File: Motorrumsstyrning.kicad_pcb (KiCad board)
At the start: 4 copper layers, 65 x 60.5 mm, 59 parts, among them J1 SD_Card_Connector, J10 Jumper, J11 Jumper, J12 Jumper, J13 Jumper, J14 Jumper, J15 Jumper, J16 Jumper, J17 Jumper, J18 Jumper, J19 Jumper, J2 Jumper, J20 Jumper, J21 Jumper, J22 Jumper, J23 Screw_Terminal_01x10, J24 Screw_Terminal_01x10, J3 Jumper, J4 Jumper, J5 Jumper, J6 Jumper, J7 Jumper, J8 Jumper, J9 Jumper, Q1 BC337, Q2 BC337, U1 NUCLEO-F303K8, U2 LM1084-5.0, U3 MCP2551-I-P

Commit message: Vidareutveckling
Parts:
- removed G***: LOGO, Vera-MRS-21:Vera-Logo-Small
- removed the J10 at (139.7, 113.0)
- removed the J14 at (144.8, 114.9)
- removed the J15 at (147.3, 114.9)
- removed J16, J17, J18, J19, J20, J21, J22: Jumper, Vera-MRS-21:THT_Jumper
- added J13: Conn_01x11, Connector_PinHeader_2.54mm:PinHeader_1x11_P2.54mm_Vertical, F.Cu at (137.2, 114.9)
- moved JP2 0.13 mm to (144.8, 112.5)
- moved JP3 0.13 mm to (147.3, 112.5)
- moved JP4 0.13 mm to (149.9, 112.5)
- moved JP5 0.13 mm to (152.4, 112.5)
- moved JP6 0.13 mm to (154.9, 112.5)
- moved JP7 0.13 mm to (157.5, 112.5)
- moved JP8 0.13 mm to (160.0, 112.5)
- moved JP9 0.13 mm to (162.6, 112.5)
- renumbered J11 to J10, J12 to J11, J13 to J12, J23 to J14, J24 to J15
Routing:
- net +5V: track 74.9 -> 83.4 mm
- net /USART2_TX: track 32.0 -> 27.1 mm, vias 1 -> 0
- net /USART2_RX: track 30.8 -> 27.9 mm, vias 1 -> 0
- net /AREF: track 11.4 -> 13.1 mm
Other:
- board text added: "MRS Rev. A Axel Henriksson Erik Bångsbo"
- board text removed: "Rev. A Axel Henriksson Erik Bångsbo"

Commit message: Removed old code, generated new for F303K8
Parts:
- removed JP2, JP3: SolderJumper_2_Bridged, Jumper:SolderJumper-2_P1.3mm_Bridged2Bar_RoundedPad1.0x1.5mm
- J13: value Conn_01x11 -> Conn_01x09; footprint Connector_PinHeader_2.54mm:PinHeader_1x11_P2.54mm_Vertical -> Connector_PinHeader_2.54mm:PinHeader_1x09_P2.54mm_Vertical
- moved J13 5.08 mm to (142.2, 114.9)
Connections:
- net /USART2_RX renamed /USART1_RX
- net /USART2_TX renamed /USART1_TX
- J13 pad 1: +5V -> /AREF
- J13 pad 2: GND -> +5V
- J13 pad 3: /AREF -> GND
- J14 pad 1: Net-(J13-Pad4) -> +5V
- J14 pad 2: Net-(J13-Pad5) -> GND
- J14 pad 3: Net-(J13-Pad6) -> Net-(J13-Pad4)
- J14 pad 4: Net-(J13-Pad7) -> Net-(J13-Pad5)
- J14 pad 5: Net-(J13-Pad8) -> Net-(J13-Pad6)
- J14 pad 6: Net-(J13-Pad9) -> Net-(J13-Pad7)
- J14 pad 7: Net-(J13-Pad10) -> Net-(J13-Pad8)
- J14 pad 8: Net-(J13-Pad11) -> Net-(J13-Pad9)
- JP4 pad 1: /PA0 -> /PB3
- JP4 pad 2: Net-(J13-Pad6) -> Net-(J13-Pad4)
- JP5 pad 1: /PA1 -> /PA0
- JP5 pad 2: Net-(J13-Pad7) -> Net-(J13-Pad5)
- JP6 pad 1: /PA3 -> /PA1
- JP6 pad 2: Net-(J13-Pad8) -> Net-(J13-Pad6)
- JP7 pad 1: /PA4 -> /PA3
- JP7 pad 2: Net-(J13-Pad9) -> Net-(J13-Pad7)
- JP8 pad 2: Net-(J13-Pad10) -> Net-(J13-Pad8)
- JP9 pad 2: Net-(J13-Pad11) -> Net-(J13-Pad9)
- R14 pad 2: /Start_Enable -> (no net)
- U1 pad CN3_10: /Deadmans -> (no net)
- U1 pad CN3_11: /Tachometer -> /Deadmans
- U1 pad CN3_12: /PA8 -> /Tachometer
- U1 pad CN3_14: /Start_Enable -> (no net)
- U1 pad CN4_1: Net-(U1-PadCN4_1) -> (no net)
- U1 pad CN4_5: /Injector_Enable -> (no net)
- U1 pad CN4_9: /PA4 -> /Injector_Enable
- U3 pad 5: Net-(U3-Pad5) -> (no net)
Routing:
- net /PA8: track 18.3 -> 0.00 mm
- net /Start_Enable: track 11.8 -> 0.00 mm
- net (no net): track 0.00 -> 11.8 mm
- net +5V: track 83.4 -> 91.8 mm
- net Net-(J13-Pad11): track 6.84 -> 0.00 mm
- net Net-(J13-Pad10): track 6.84 -> 0.00 mm
- net /Injector_Enable: track 4.97 -> 11.5 mm
- net /AREF: track 13.1 -> 7.18 mm
- net /PB3: track 3.38 -> 8.46 mm
- net /SPI1_MOSI: track 45.0 -> 41.2 mm
- net /PA4: track 2.02 -> 0.00 mm
- net /PA3: track 2.02 -> 3.38 mm
- net /PA1: track 2.02 -> 3.38 mm
- net /PA0: track 2.02 -> 3.38 mm
- net /Tachometer: track 8.56 -> 7.51 mm

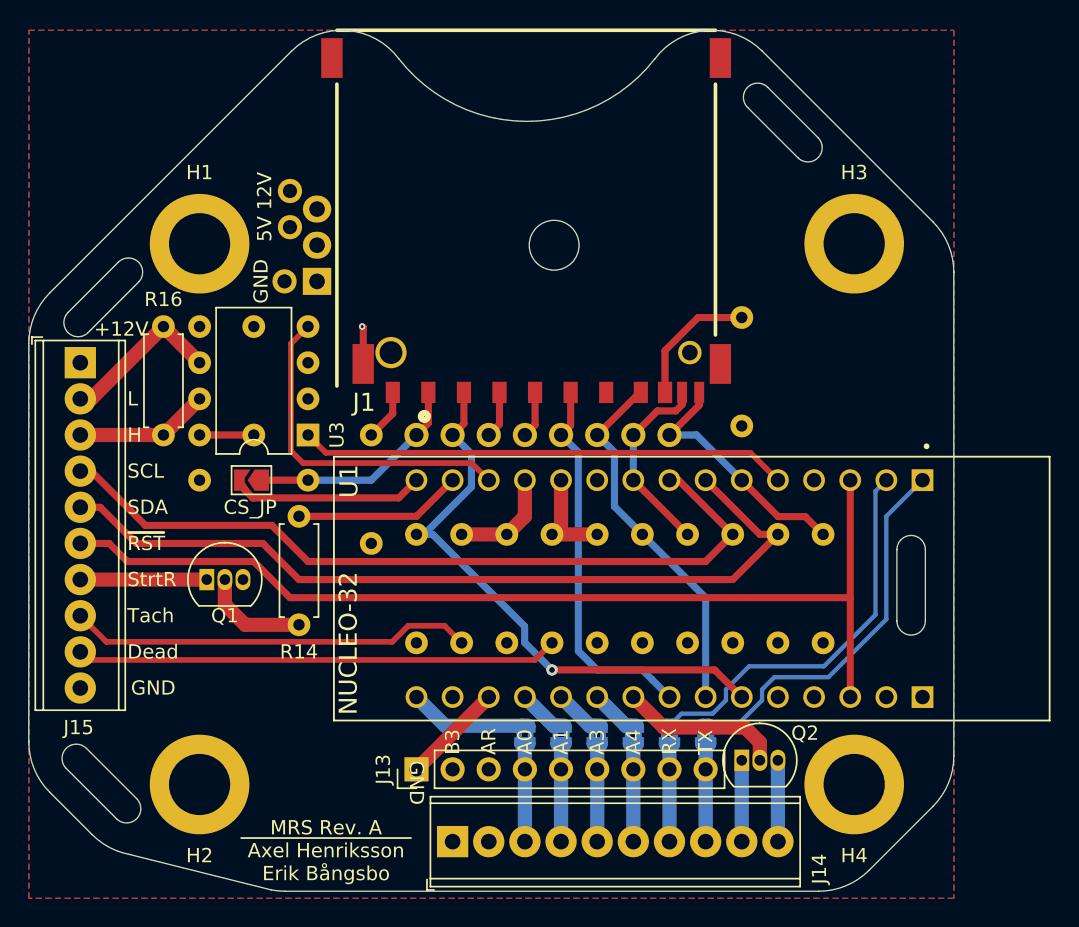
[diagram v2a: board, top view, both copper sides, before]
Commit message: Fixed Silkscreen
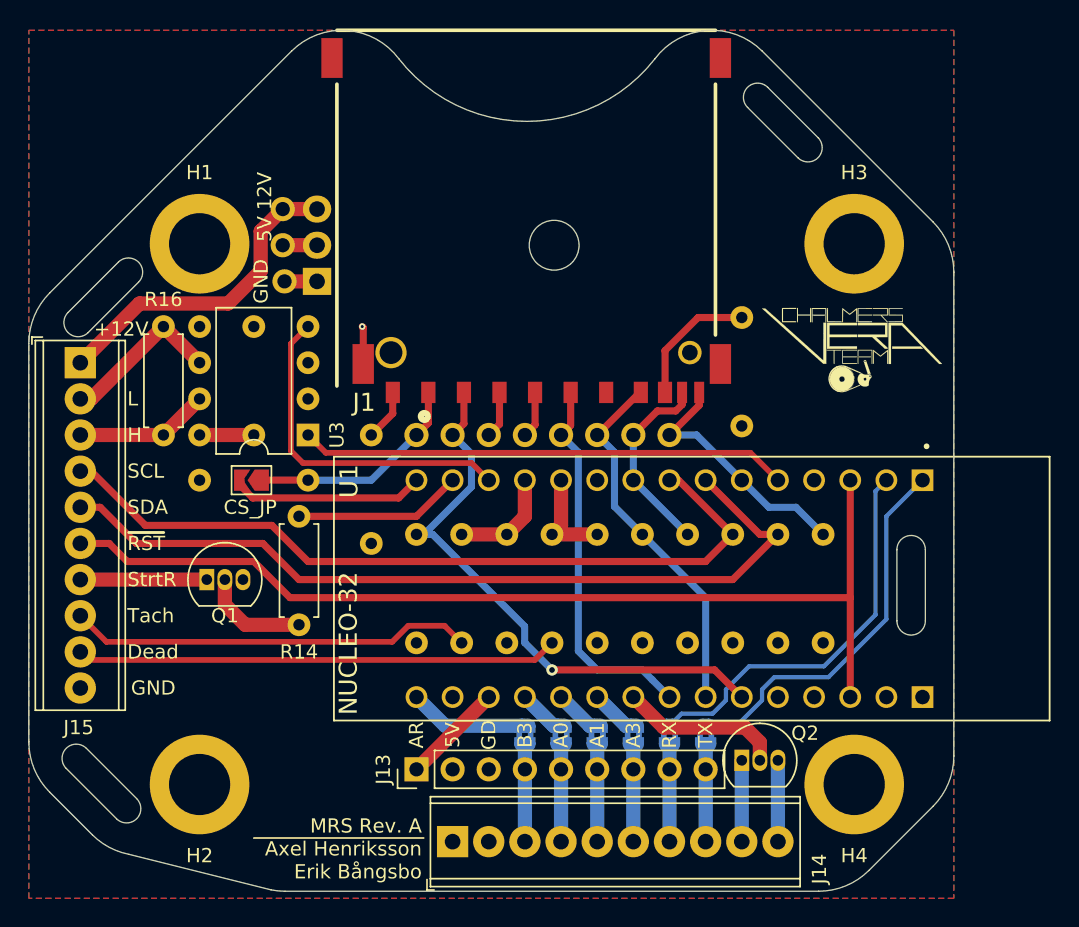
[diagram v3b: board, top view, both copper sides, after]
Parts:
- added G***: LOGO, Vera-MRS-21:Vera-Logo-Small, B.Cu at (173.0, 85.5)
- added G***: LOGO, Vera-MRS-21:Vera-Logo-Small, F.Cu at (172.8, 85.5)
- moved J12 1.37 mm to (132.8, 78.1)
- moved J10 1.37 mm to (132.8, 75.6)
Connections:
- R14 pad 2: (no net) -> /Start_Enable
- U1 pad CN3_14: (no net) -> /Start_Enable
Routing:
- net /Start_Enable: track 0.00 -> 11.8 mm
- net (no net): track 11.8 -> 0.00 mm
- net GND: track 6.15 -> 8.43 mm
- net +12V: track 24.3 -> 22.8 mm
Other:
- board text added: "+5V"
- board text added: "GD"
- board text removed: "A4"
- board text removed: "ARF"
- board text removed: "PA4"

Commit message: Finalization and Gerber generation
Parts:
- removed the G*** at (173.0, 85.5)
- removed the G*** at (172.8, 85.5)
- removed the U2 at (135.3, 80.6)
- added C1: 0.33u, Capacitor_SMD:C_1206_3216Metric_Pad1.42x1.75mm_HandSolder, B.Cu at (133.1, 73.0)
- added C2: 0.1u, Capacitor_SMD:C_1206_3216Metric_Pad1.42x1.75mm_HandSolder, B.Cu at (137.2, 71.5)
- added G***: LOGO, Vera-MRS-21:Pb, B.Cu at (134.6, 111.8)
- added G***: LOGO, Vera-MRS-21:Vera-Logo-Small, B.Cu at (173.2, 87.0)
- added G***: LOGO, Vera-MRS-21:Vera-Logo-Small, F.Cu at (172.7, 85.3)
- added U1: LM1084-5.0, Package_TO_SOT_THT:TO-220-3_Horizontal_TabDown, B.Cu at (135.3, 80.6)
- renumbered J10 to J1, J8 to J10, J9 to J11, J1 to J12, J2 to J13, J13 to J14, J14 to J15, J12 to J2, J11 to J3, J3 to J4, J15 to J5, J4 to J6, J5 to J7, J6 to J8, J7 to J9, JP4 to JP2, JP5 to JP3, JP6 to JP4, JP7 to JP5, JP8 to JP6, JP9 to JP7, R14 to R1, R5 to R10, R6 to R11, R7 to R12, R8 to R13, R9 to R14, R12 to R15, R13 to R16, R16 to R2, R15 to R3, R2 to R4, R10 to R5, R11 to R6, R1 to R7, R3 to R8, R4 to R9, U3 to U2, U1 to U3
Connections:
- J14 pad 1: /AREF -> +3V3
- U3 pad CN4_13: /AREF -> (no net)
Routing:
- net /AREF: track 7.18 -> 0.00 mm
- net +3V3: track 3.29 -> 9.42 mm
- net +5V: track 91.8 -> 97.7 mm
- net +12V: track 22.8 -> 25.6 mm
- net GND: track 8.43 -> 5.77 mm, vias 1 -> 0
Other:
- outline, holes or cut-outs redrawn
- board text added: "3V"
- board text added: "Github.com/AxelHenriksson/Vera-MRS-21"
- board text added: "JLCJLCJLCJLC"
- board text added: "MRS 2021 Erik Bångsbo Axel Henriksson"
- board text added: "Rev. A"
- board text removed: "AR"
- board text removed: "MRS Rev. A Axel Henriksson Erik Bångsbo"
